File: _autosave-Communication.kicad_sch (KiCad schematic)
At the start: 52 parts, among them J2 Conn_02x05_Odd_Even, J3 USB_A_Stacked, J4 USB_A_Stacked, U1 IMX6UL, U10 FE2.1, U8 X1000, Y1 12MHz

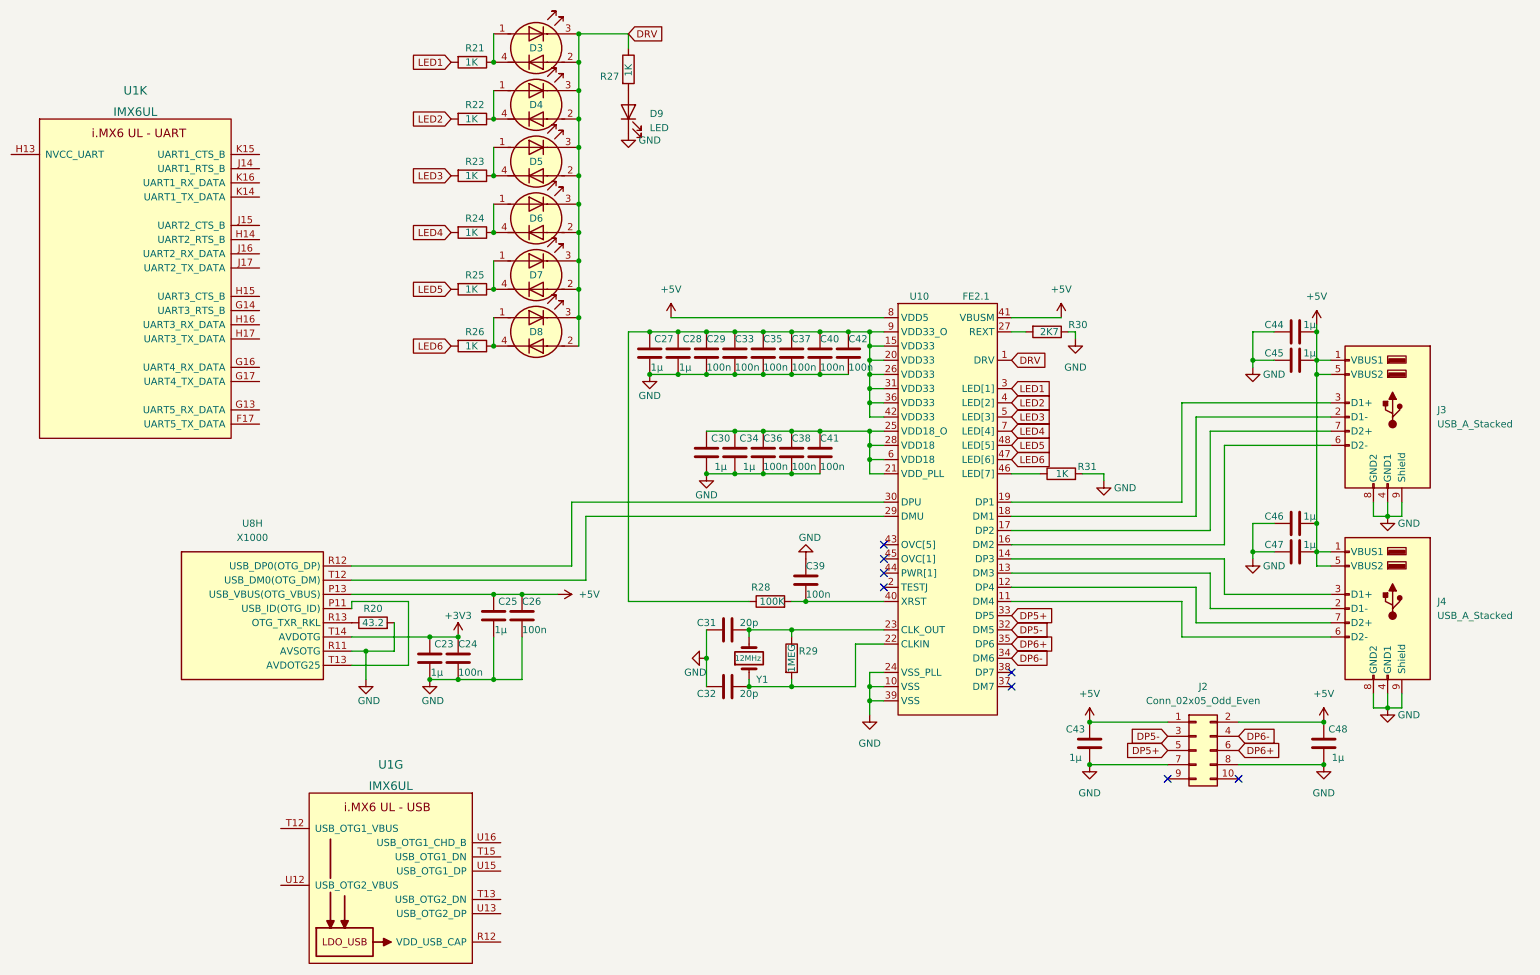
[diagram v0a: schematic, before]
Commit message: Display Update
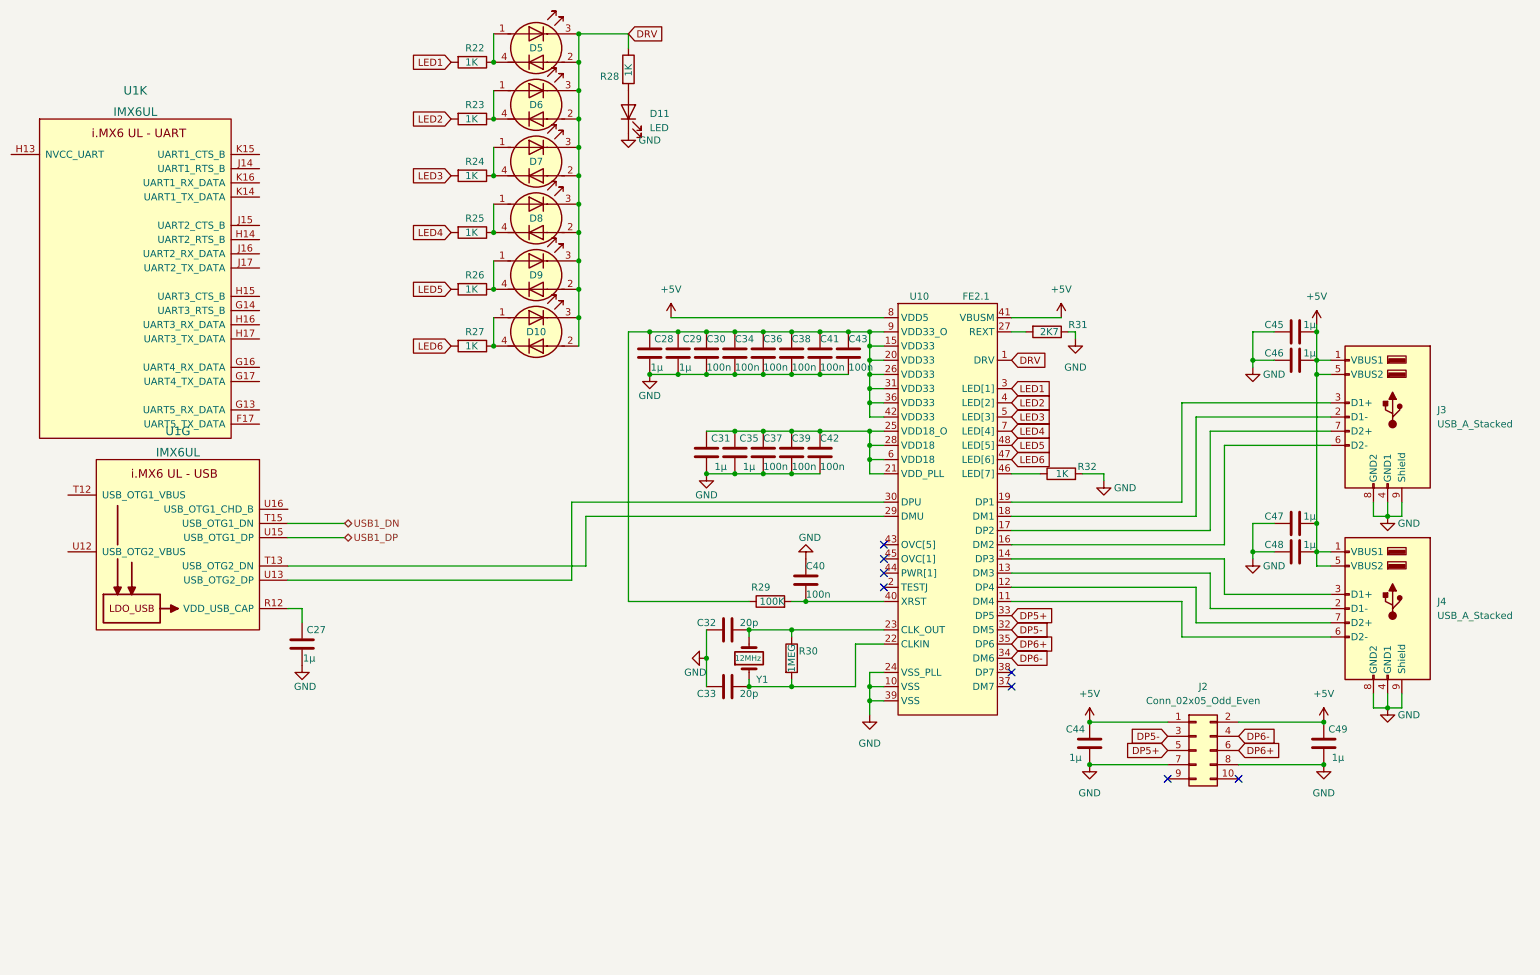
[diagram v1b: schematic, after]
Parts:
- removed C23, C25: 1µ, Capacitor_SMD:C_0402_1005Metric, symbol Device:C
- removed C24, C26: 100n, Capacitor_SMD:C_0402_1005Metric, symbol Device:C
- removed R20: 43.2, Resistor_SMD:R_0402_1005Metric, symbol Device:R
- removed U8: X1000, TheBrutzlers_Lib:BGA256C80P16X16_1300X1300X130N, symbol TheBrutzlers_Lib:X1000
- added C27: 1µ, Capacitor_SMD:C_0402_1005Metric, symbol Device:C
- renumbered C27 to C28, C28 to C29, C29 to C30, C30 to C31, C31 to C32, C32 to C33, C33 to C34, C34 to C35, C35 to C36, C36 to C37, C37 to C38, C38 to C39, C39 to C40, C40 to C41, C41 to C42, C42 to C43, C43 to C44, C44 to C45, C45 to C46, C46 to C47, C47 to C48, C48 to C49, D8 to D10, D9 to D11, D3 to D5, D4 to D6, D5 to D7, D6 to D8, D7 to D9, R21 to R22, R22 to R23, R23 to R24, R24 to R25, R25 to R26, R26 to R27, R27 to R28, R28 to R29, R29 to R30, R30 to R31, R31 to R32
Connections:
- net GND: now also C27.2
- net at U1.R12 (VDD_USB_CAP): now also C27.1
- net at U1.T13 (USB_OTG2_DN): now also U10.29 (DMU)
- net USB1_DN: now reaches U1.T15 (USB_OTG1_DN)
- net at U1.U13 (USB_OTG2_DP): now also U10.30 (DPU)
- net USB1_DP: now reaches U1.U15 (USB_OTG1_DP)
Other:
- moved on the sheet: U1G
